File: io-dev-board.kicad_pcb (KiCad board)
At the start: 2 copper layers, 95.5 x 57.5 mm, 67 parts, among them IC1 24LC01B_P, J1 PWR, J2 SW_Conn, J3 LED_Conn, J4 I2C_Conn, J5 Rot_Conn, Q1 Q_NPN, Q2 Q_NPN, Q3 Q_NPN, Q4 Q_NPN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

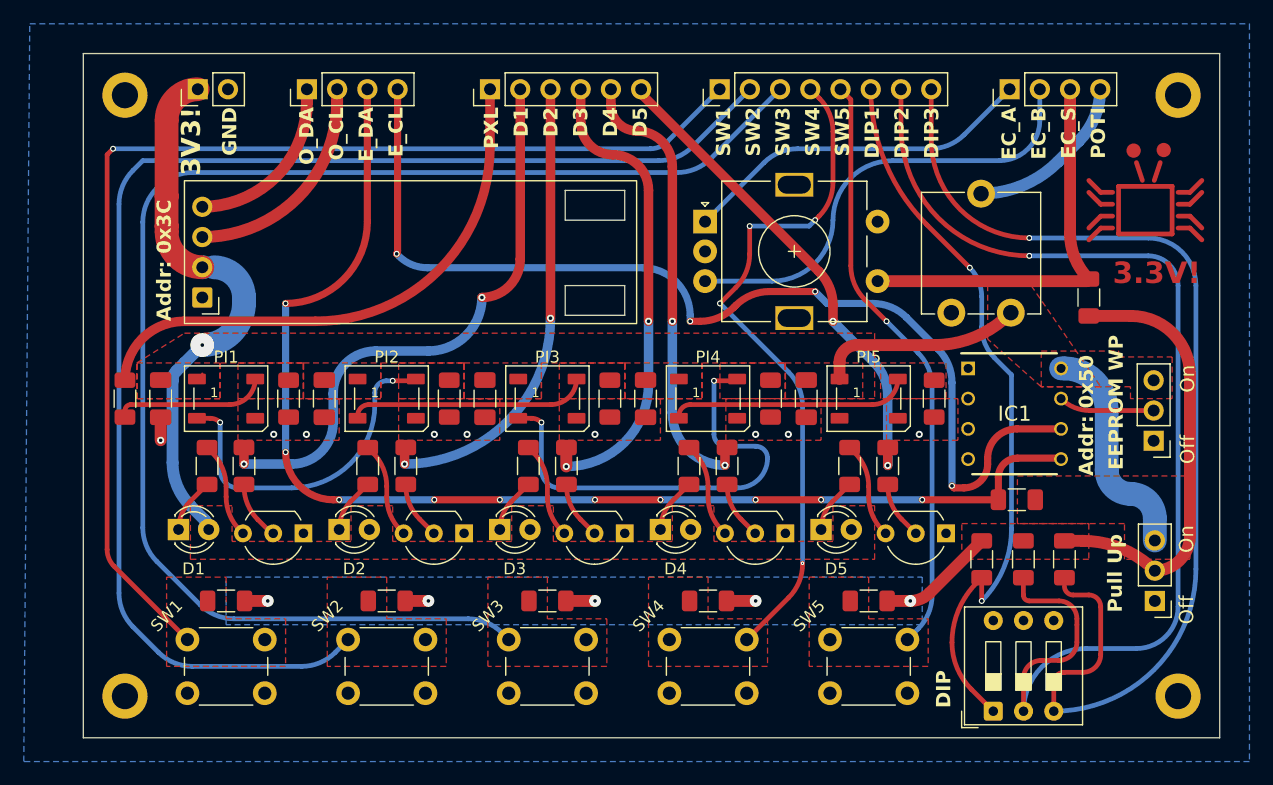
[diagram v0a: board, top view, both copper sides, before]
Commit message: refactor: align transistors with LEDs
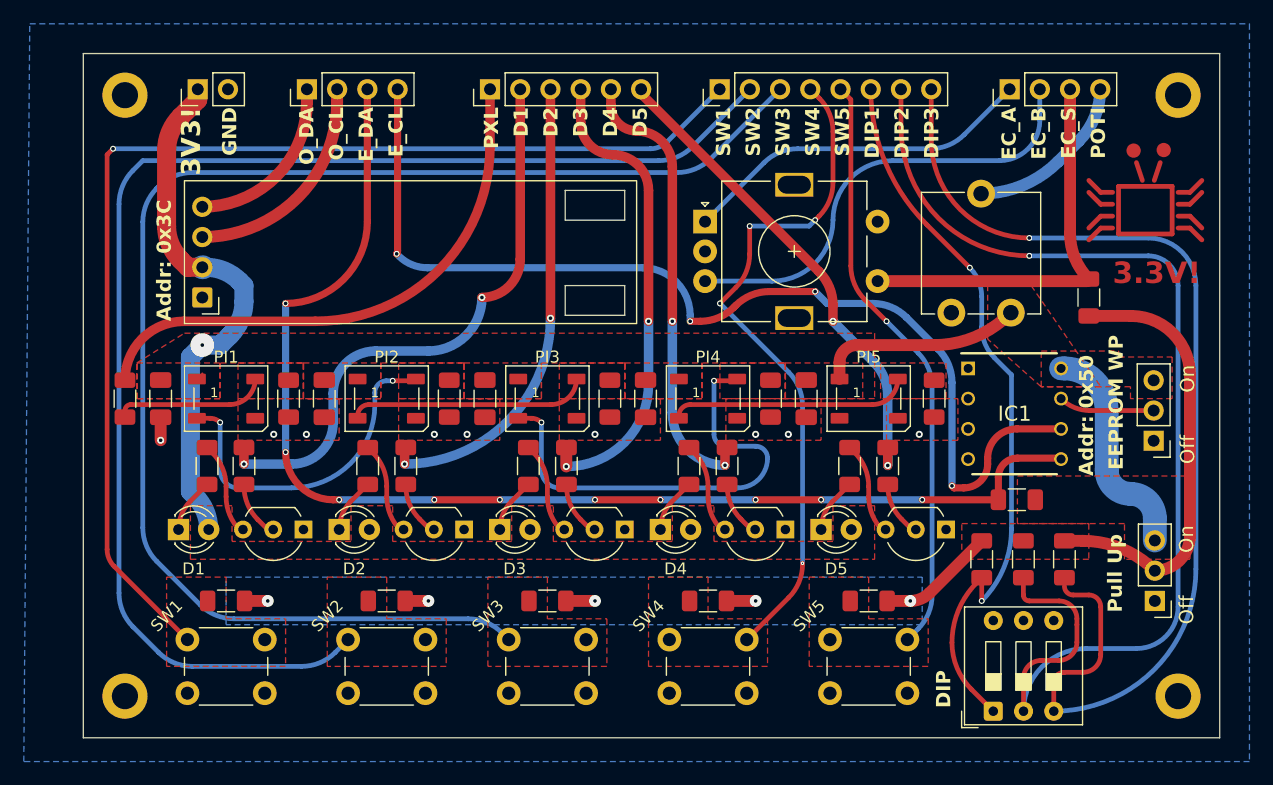
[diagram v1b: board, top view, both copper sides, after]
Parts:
- moved Q1 0.32 mm to (95.0, 111.0)
- moved Q2 0.32 mm to (108.5, 111.0)
- moved Q3 0.32 mm to (122.0, 111.0)
- moved Q4 0.32 mm to (135.5, 111.0)
- moved Q5 0.32 mm to (149.0, 111.0)
